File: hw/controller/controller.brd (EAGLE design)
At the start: 46 x 53 mm, 127 parts, among them J1 XT30XT30PW_MALE, J2 XT30XT30PW_MALE, M1 MOUNT, M2 MOUNT, M3 MOUNT, M4 MOUNT, Q1 TPH1R204PLSOP_ADVANCE_8, Q2 TPH1R204PLSOP_ADVANCE_8, Q3 TPH1R204PLSOP_ADVANCE_8, Q4 TPH1R204PLSOP_ADVANCE_8, Q5 TPH1R204PLSOP_ADVANCE_8, Q6 TPH1R204PLSOP_ADVANCE_8, U1 STM32G474CEU6, U2 TCAN334GSOT23, U3 AS5147, U4 MAX15062AATA+T, U5 DRV8353S

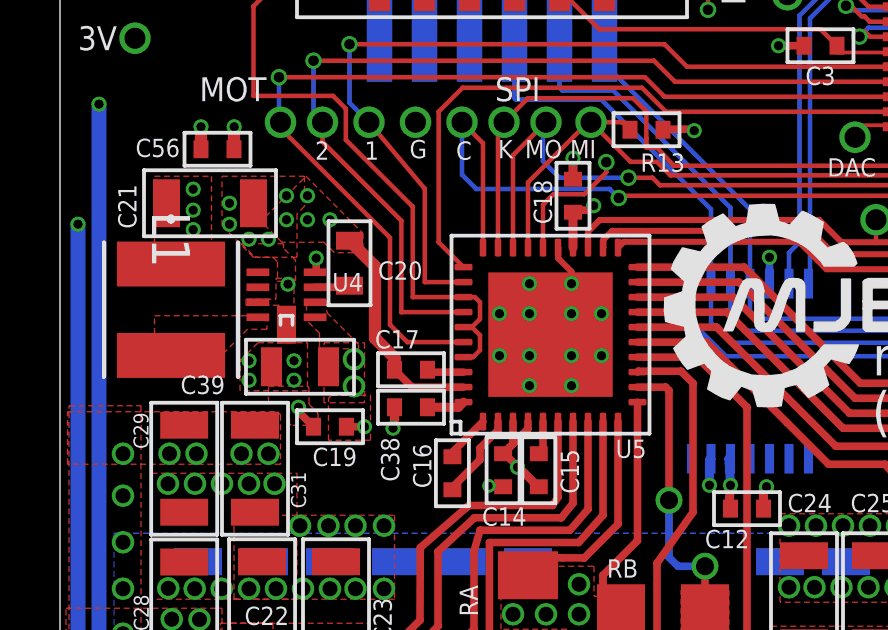
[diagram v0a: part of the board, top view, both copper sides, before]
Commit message: r4.6: Connect the DRV8353F gnd to the power ground
It had previously been connected to the logic ground, but I think it
is actually used for the high power things.
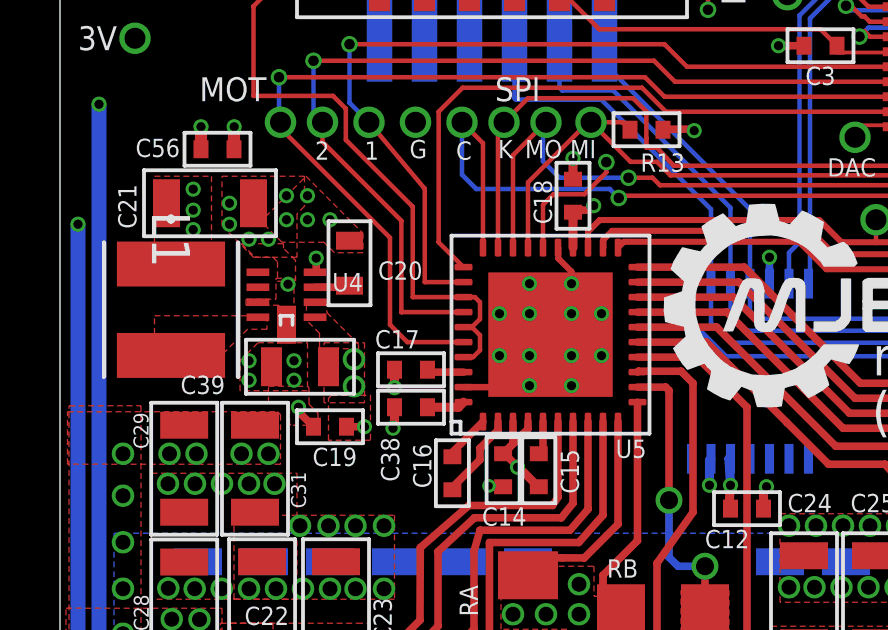
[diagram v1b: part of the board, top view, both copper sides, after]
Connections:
- net GND: no longer C17.P$1, U5.39
- net V-: now also C17.P$1, U5.39
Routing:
- net GND: track 121.7 -> 114.2 mm
- net V-: track 11.6 -> 14.4 mm, vias 70 -> 71
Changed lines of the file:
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@@
 <via x="-16.7" y="-8.3" extent="1-16" drill="0.3048"/>
 <via x="-16.7" y="-7.65" extent="1-16" drill="0.3048"/>
+<contactref element="U5" pad="39"/>
+<contactref element="C17" pad="P$1"/>
+<wire x1="-9.55" y1="-8.53" x2="-7.4" y2="-8.53" width="0.2159" layer="1"/>
+<wire x1="-7.4" y1="-8.53" x2="-7.35" y2="-8.48" width="0.254" layer="1"/>
+<via x="-11.85" y="-8.55" extent="1-16" drill="0.3048"/>
+<wire x1="-11.85" y1="-7.95" x2="-11.85" y2="-8.55" width="0.3048" layer="1"/>
 </signal>
 <signal name="CUR3">
@@
 <wire x1="7.15" y1="-32.85" x2="8.5328875" y2="-32.85" width="0.4064" layer="16"/>
 <contactref element="U1" pad="29"/>
-<contactref element="C17" pad="P$1"/>
-<contactref element="U5" pad="39"/>
 <contactref element="U4" pad="7"/>
 <contactref element="C21" pad="P$2"/>
@@
 <wire x1="-8.7" y1="4.75" x2="-9.3" y2="4.75" width="0.254" layer="1"/>
 <wire x1="-9.35" y1="4.7" x2="-9.3" y2="4.75" width="0.254" layer="1"/>
-<wire x1="-11.85" y1="-7.95" x2="-11.27" y2="-8.53" width="0.254" layer="1"/>
-<wire x1="-11.27" y1="-8.53" x2="-9.55" y2="-8.53" width="0.254" layer="1"/>
 <via x="12.7" y="2.15" extent="1-16" drill="0.3048"/>
 <wire x1="11.75" y1="2.15" x2="12.7" y2="2.15" width="0.254" layer="1"/>
 <via x="-15.4" y="-5.1" extent="1-16" drill="0.3048"/>
 <wire x1="-13.35" y1="-3.65" x2="-13.65" y2="-3.65" width="0.3048" layer="1"/>
-<wire x1="-11.85" y1="-7.95" x2="-11.85" y2="-7.55" width="0.4064" layer="1"/>
-<wire x1="-11.85" y1="-7.55" x2="-12.5" y2="-6.9" width="0.4064" layer="1"/>
-<wire x1="-12.5" y1="-4.5" x2="-13.35" y2="-3.65" width="0.4064" layer="1"/>
-<wire x1="-12.5" y1="-6.9" x2="-12.5" y2="-4.5" width="0.4064" layer="1"/>
 <wire x1="-9.35" y1="5.15" x2="-9.1" y2="5.15" width="0.254" layer="16"/>
 <wire x1="-9.1" y1="5.15" x2="-8.7" y2="4.75" width="0.254" layer="16"/>

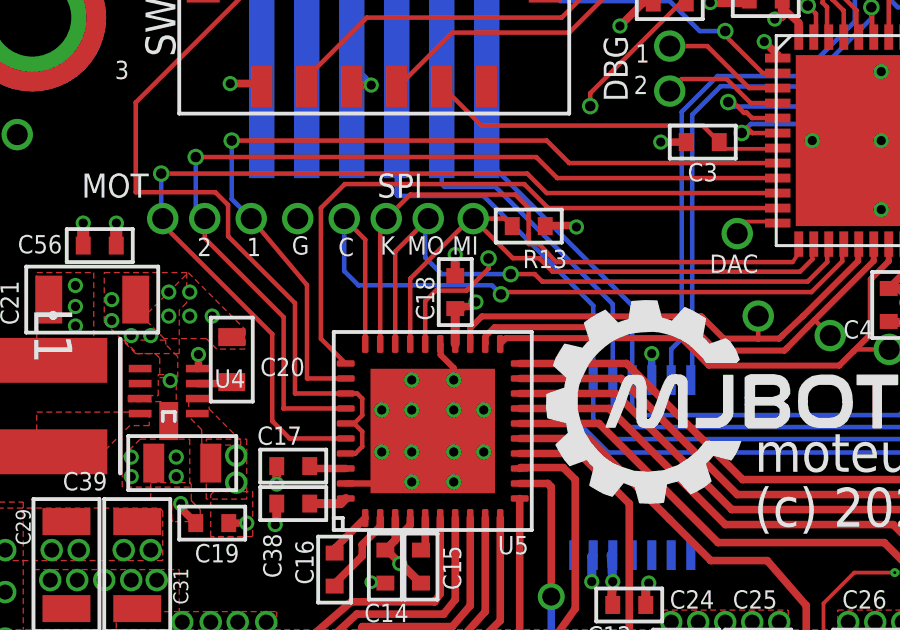
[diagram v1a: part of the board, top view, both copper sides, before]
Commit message: r4.6: And actually connect the AGND to the logic ground
The datasheet shows all the current sense outputs as relative to this
ground and VREF, so it definitely needs to be connected here.
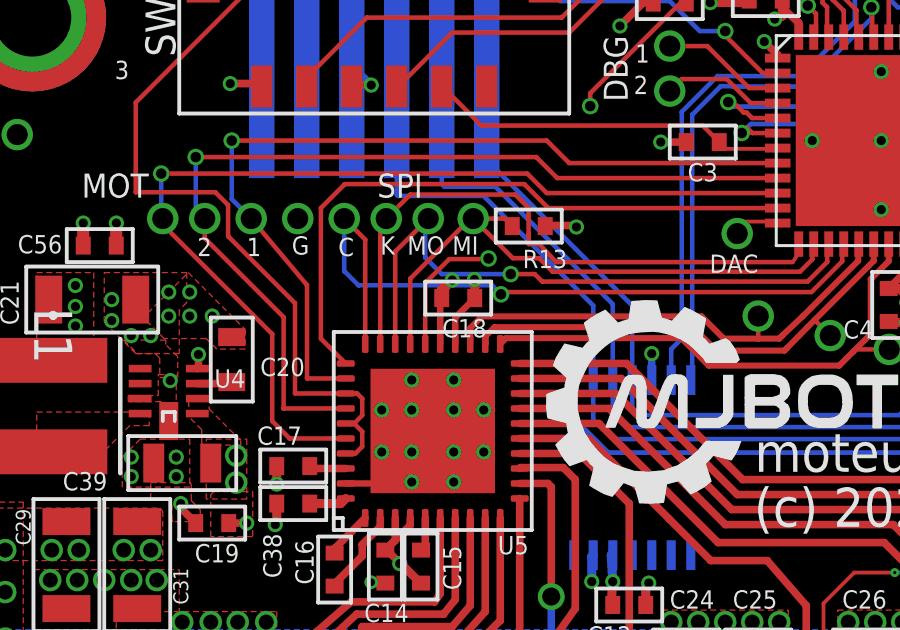
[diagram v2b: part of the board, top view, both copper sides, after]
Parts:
- moved C18 0.22 mm to (-5.80, -2.35), turned to 0 degrees
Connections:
- net GND: now also U5.25
- net V-: no longer U5.25
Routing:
- net GND: track 114.2 -> 115.8 mm
- net V-: track 14.4 -> 13.1 mm
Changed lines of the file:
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@@
 <layer number="21" name="tPlace" color="7" fill="1" visible="yes" active="yes"/>
 <layer number="22" name="bPlace" color="7" fill="1" visible="yes" active="yes"/>
-<layer number="23" name="tOrigins" color="15" fill="1" visible="no" active="yes"/>
-<layer number="24" name="bOrigins" color="15" fill="1" visible="yes" active="yes"/>
+<layer number="23" name="tOrigins" color="15" fill="1" visible="yes" active="yes"/>
+<layer number="24" name="bOrigins" color="15" fill="1" visible="no" active="yes"/>
 <layer number="25" name="tNames" color="7" fill="1" visible="yes" active="yes"/>
 <layer number="26" name="bNames" color="7" fill="1" visible="yes" active="yes"/>
@@
 <attribute name="VOLTAGE" value="" x="-7.04" y="-11.3" size="1.778" layer="27" rot="R90" display="off"/>
 </element>
-<element name="C18" library="mfpassives" package="C0402" value="0.1uF" x="-5.9" y="-2.15" smashed="yes" rot="R270">
-<attribute name="DIELECTRIC" value="" x="-5.9" y="-2.15" size="1.778" layer="27" rot="R270" display="off"/>
-<attribute name="HOUSEPART" value="YES" x="-5.9" y="-2.15" size="1.778" layer="27" rot="R270" display="off"/>
-<attribute name="MF" value="" x="-5.9" y="-2.15" size="1.778" layer="27" rot="R270" display="off"/>
-<attribute name="MPN" value="MF-CAP-0402-0.1uF" x="-5.9" y="-2.15" size="1.778" layer="27" rot="R270" display="off"/>
-<attribute name="NAME" x="-6.6" y="-3.1" size="0.6096" layer="25" font="vector" ratio="10" rot="R90"/>
-<attribute name="POPULATE" value="1" x="-5.9" y="-2.15" size="1.778" layer="27" rot="R270" display="off"/>
-<attribute name="TOLERANCE" value="" x="-5.9" y="-2.15" size="1.778" layer="27" rot="R270" display="off"/>
-<attribute name="URL" value="" x="-5.9" y="-2.15" size="1.778" layer="27" rot="R270" display="off"/>
-<attribute name="VOLTAGE" value="" x="-5.9" y="-2.15" size="1.778" layer="27" rot="R270" display="off"/>
+<element name="C18" library="mfpassives" package="C0402" value="0.1uF" x="-5.8" y="-2.35" smashed="yes">
+<attribute name="DIELECTRIC" value="" x="-5.8" y="-2.35" size="1.778" layer="27" display="off"/>
+<attribute name="HOUSEPART" value="YES" x="-5.8" y="-2.35" size="1.778" layer="27" display="off"/>
+<attribute name="MF" value="" x="-5.8" y="-2.35" size="1.778" layer="27" display="off"/>
+<attribute name="MPN" value="MF-CAP-0402-0.1uF" x="-5.8" y="-2.35" size="1.778" layer="27" display="off"/>
+<attribute name="NAME" x="-4.85" y="-3.05" size="0.6096" layer="25" font="vector" ratio="10" rot="R180"/>
+<attribute name="POPULATE" value="1" x="-5.8" y="-2.35" size="1.778" layer="27" display="off"/>
+<attribute name="TOLERANCE" value="" x="-5.8" y="-2.35" size="1.778" layer="27" display="off"/>
+<attribute name="URL" value="" x="-5.8" y="-2.35" size="1.778" layer="27" display="off"/>
+<attribute name="VOLTAGE" value="" x="-5.8" y="-2.35" size="1.778" layer="27" display="off"/>
 </element>
 <element name="C17" library="mfpassives" package="C0402" value="1uF" x="-11.3" y="-7.95" smashed="yes">
@@
 <via x="-18.56" y="-3.28" extent="1-16" drill="0.3048"/>
 <contactref element="ENC" pad="1"/>
-<via x="-5.21" y="-2.48" extent="1-16" drill="0.3048"/>
-<wire x1="-5.7" y1="-2.7" x2="-5.9" y2="-2.7" width="0.254" layer="1"/>
-<wire x1="-5.63" y1="-2.63" x2="-5.7" y2="-2.7" width="0.254" layer="1"/>
-<wire x1="-5.36" y1="-2.63" x2="-5.63" y2="-2.63" width="0.254" layer="1"/>
-<wire x1="-5.36" y1="-2.63" x2="-5.21" y2="-2.48" width="0.254" layer="1"/>
+<via x="-5.26" y="-1.73" extent="1-16" drill="0.3048"/>
+<wire x1="-5.25714375" y1="-2.35" x2="-5.25" y2="-2.35" width="0.254" layer="1"/>
 <polygon width="0.1524" layer="1" thermals="no">
 <vertex x="-19.85" y="-1.5"/>
@@
 <wire x1="-12.35" y1="5.15" x2="-12.7" y2="4.8" width="0.254" layer="16"/>
 <wire x1="-12.7" y1="4.8" x2="-13.4" y2="4.8" width="0.254" layer="16"/>
-<wire x1="-5.9" y1="-3.88" x2="-5.9" y2="-2.7" width="0.3048" layer="1"/>
 <contactref element="C56" pad="P$1"/>
 <via x="-17.195" y="0.15" extent="1-16" drill="0.3048"/>
@@
 <wire x1="-17.2" y1="-0.6" x2="-17.2" y2="0.145" width="0.4064" layer="1"/>
 <wire x1="-17.2" y1="0.145" x2="-17.195" y2="0.15" width="0.4064" layer="1"/>
+<wire x1="-5.9" y1="-3.88" x2="-5.9" y2="-3" width="0.2159" layer="1"/>
+<wire x1="-5.9" y1="-3" x2="-5.25" y2="-2.35" width="0.2159" layer="1"/>
+<wire x1="-5.25" y1="-2.35" x2="-5.25" y2="-1.74" width="0.3048" layer="1"/>
+<wire x1="-5.25" y1="-1.74" x2="-5.26" y2="-1.73" width="0.3048" layer="1"/>
 </signal>
 <signal name="NRST">
@@
 <contactref element="U5" pad="P14"/>
 <contactref element="U5" pad="P18"/>
-<contactref element="U5" pad="25"/>
 <contactref element="C39" pad="P$2"/>
 <wire x1="-6.65" y1="-6.78" x2="-5.95" y2="-7.48" width="0.254" layer="1"/>
-<wire x1="-6.4" y1="-3.88" x2="-6.3886" y2="-3.8914" width="0.2032" layer="1"/>
-<wire x1="-6.3886" y1="-3.8914" x2="-6.3886" y2="-4.24246875" width="0.2032" layer="1"/>
-<wire x1="-5.95" y1="-4.68106875" x2="-5.95" y2="-5.08" width="0.2032" layer="1"/>
-<wire x1="-6.3886" y1="-4.24246875" x2="-5.95" y2="-4.68106875" width="0.2032" layer="1"/>
 <polygon width="0.1524" layer="1" isolate="0.5" thermals="no">
 <vertex x="-17" y="-7.65"/>
@@
 <wire x1="1.62016875" y1="7.5" x2="1.8" y2="7.5" width="0.127" layer="1"/>
 <contactref element="U5" pad="26"/>
-<wire x1="-6.9" y1="-3.88" x2="-6.9" y2="-2.45" width="0.1524" layer="1"/>
-<wire x1="-6.9" y1="-2.45" x2="-6.55" y2="-2.1" width="0.1524" layer="1"/>
-<wire x1="-4.79" y1="-1.37" x2="-4.79" y2="-1.0302" width="0.1524" layer="1"/>
+<wire x1="-6.9" y1="-3.88" x2="-6.9" y2="-1.85" width="0.1524" layer="1"/>
+<wire x1="-6.9" y1="-1.85" x2="-6.1" y2="-1.05" width="0.1524" layer="1"/>
+<wire x1="-4.79" y1="-1.05" x2="-4.79" y2="-1.0302" width="0.1524" layer="1"/>
 <via x="-4.79" y="-1.0302" extent="1-16" drill="0.35"/>
 <wire x1="-4.79" y1="-1.0302" x2="-1.4" y2="2.3598" width="0.1524" layer="15"/>
 <wire x1="-1.4" y1="2.3598" x2="-1.4" y2="4.05" width="0.1524" layer="15"/>
 <via x="-1.4" y="4.05" extent="1-16" drill="0.35"/>
-<wire x1="-6.55" y1="-2.1" x2="-5.52" y2="-2.1" width="0.1524" layer="1"/>
-<wire x1="-5.52" y1="-2.1" x2="-4.79" y2="-1.37" width="0.1524" layer="1"/>
+<wire x1="-6.1" y1="-1.05" x2="-4.79" y2="-1.05" width="0.1524" layer="1"/>
 <wire x1="-1.4" y1="4.47983125" x2="1.62016875" y2="7.5" width="0.1524" layer="1"/>
 <wire x1="-1.4" y1="4.05" x2="-1.4" y2="4.47983125" width="0.1524" layer="1"/>
@@
 <contactref element="C21" pad="P$2"/>
 <contactref element="C20" pad="P$2"/>
-<via x="-5.9" y="-0.9" extent="1-16" drill="0.3048"/>
-<wire x1="-5.9" y1="-0.9" x2="-5.9" y2="-1.6" width="0.3048" layer="1"/>
+<via x="-6" y="-1.75" extent="1-16" drill="0.3048"/>
+<wire x1="-6" y1="-1.75" x2="-6.25" y2="-2" width="0.3048" layer="1"/>
+<wire x1="-6.25" y1="-2" x2="-6.3" y2="-2" width="0.3048" layer="1"/>
+<wire x1="-6.3" y1="-2" x2="-6.35" y2="-2.05" width="0.3048" layer="1"/>
+<wire x1="-6.35" y1="-2.05" x2="-6.35" y2="-2.35" width="0.3048" layer="1"/>
 <via x="-17.35" y="-3.1" extent="1-16" drill="0.3048"/>
 <via x="-16.7" y="-3.6" extent="1-16" drill="0.3048"/>
@@
 </polygon>
 <via x="-14" y="-2.95" extent="1-16" drill="0.3048"/>
+<contactref element="U5" pad="25"/>
+<wire x1="-6.4" y1="-3.88" x2="-6.4" y2="-2.4" width="0.2159" layer="1"/>
+<wire x1="-6.4" y1="-2.4" x2="-6.35" y2="-2.35" width="0.2159" layer="1"/>
 </signal>
 <signal name="VTEMP_FET">

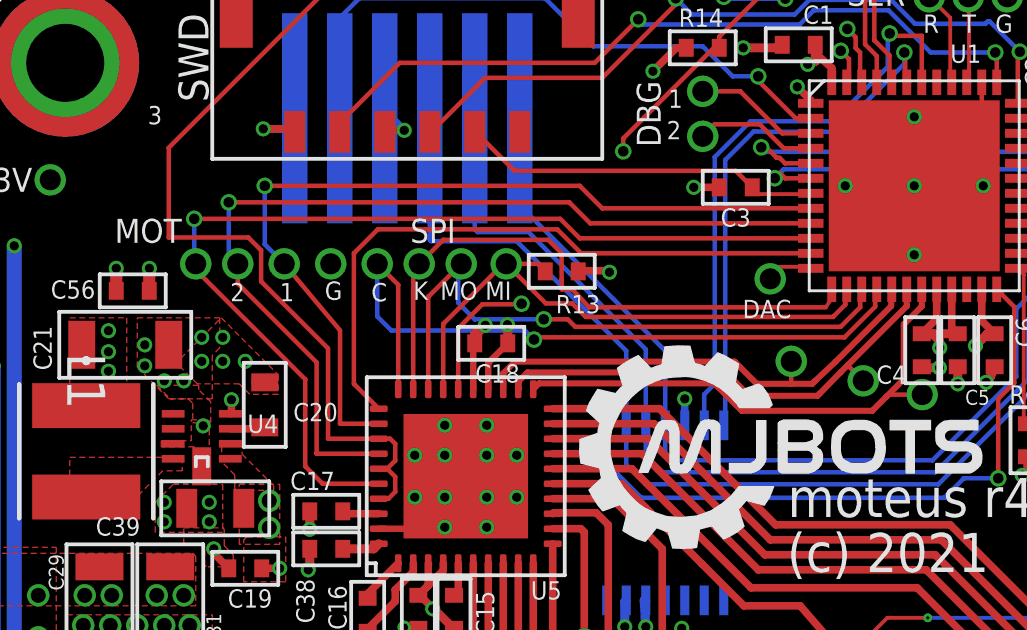
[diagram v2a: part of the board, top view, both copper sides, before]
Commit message: Scoot debug pads around to give more room for silks
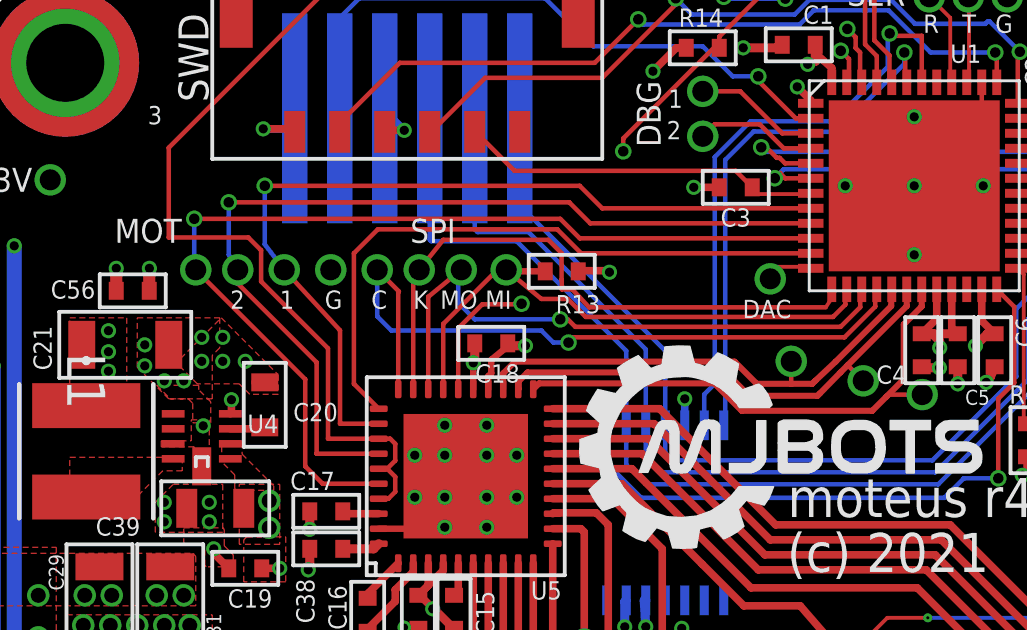
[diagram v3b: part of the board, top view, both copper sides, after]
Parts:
- moved DG1 0.20 mm to (-11.2, 0.10)
- moved DRV_CS 0.20 mm to (-9.60, 0.10)
- moved DRV_MISO 0.20 mm to (-5.30, 0.10)
- moved DRV_MOSI 0.20 mm to (-6.80, 0.10)
- moved DRV_SCK 0.20 mm to (-8.20, 0.10)
- moved MOT1 0.20 mm to (-12.7, 0.10)
- moved MOT2 0.20 mm to (-14.2, 0.10)
- moved MOT3 0.20 mm to (-15.7, 0.10)
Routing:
- net GND: track 115.8 -> 115.0 mm
